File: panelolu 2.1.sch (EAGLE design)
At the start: 24 parts, among them IC1 LM340MP-05, IC2 4050D, IC3 MCP23017SO28, SW1 EC12E_SW

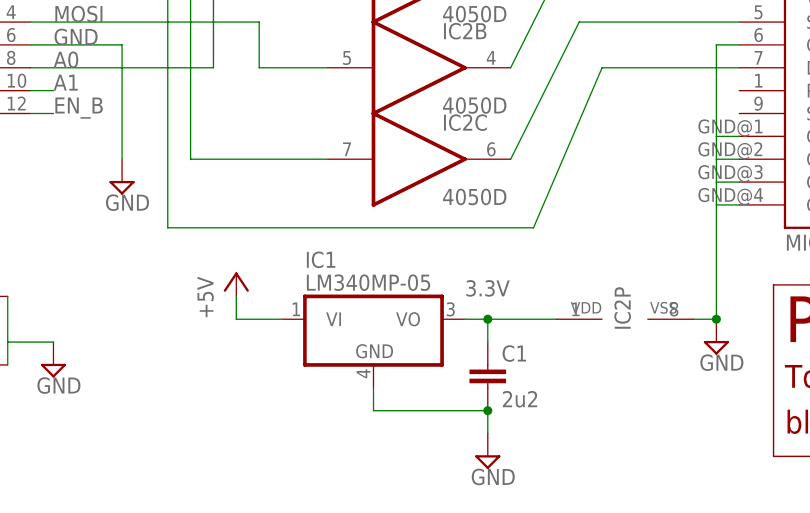
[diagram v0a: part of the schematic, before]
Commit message: Update panelolu 2.1.sch
change regulator voltage
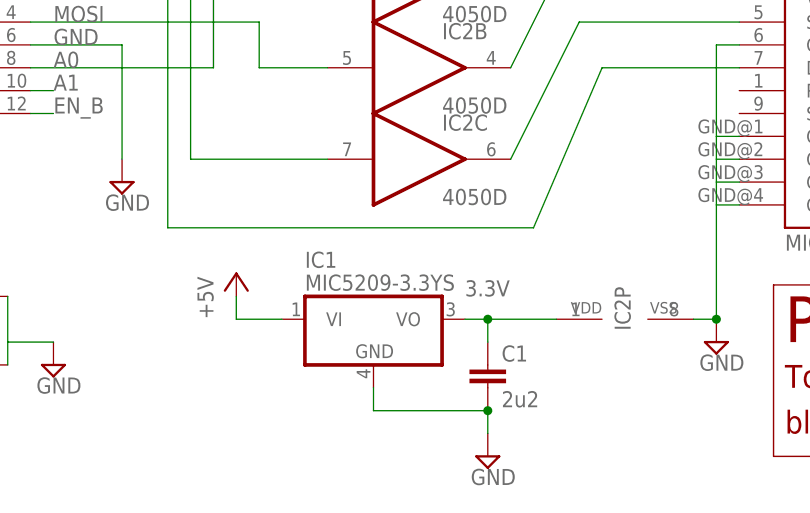
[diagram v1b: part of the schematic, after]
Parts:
- IC1: value LM340MP-05 -> MIC5209-3.3YS
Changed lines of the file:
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@@
 <?xml version="1.0" encoding="utf-8"?>
 <!DOCTYPE eagle SYSTEM "eagle.dtd">
-<eagle version="6.2">
+<eagle version="6.4">
 <drawing>
 <settings>
@@
 <parts>
 <part name="SW1" library="switch-alps" deviceset="EC12E_SW" device=""/>
-<part name="IC1" library="linear" deviceset="LM340?-*" device="MP" technology="05"/>
+<part name="IC1" library="linear" deviceset="LM340?-*" device="MP" technology="05" value="MIC5209-3.3YS"/>
 <part name="C1" library="rcl" deviceset="C-EU" device="C1206K" value="2u2"/>
 <part name="SP1" library="adafruit" deviceset="SPEAKER" device="/PS12"/>
